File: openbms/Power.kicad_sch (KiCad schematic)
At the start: 17 parts, among them Q6 BSS84AKW,115, Q7 2N7002KW, U20 LMZM23600V3

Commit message: Footprints for pmos/nmos and pmos/pmos packages fixed, charger detection added, pwr_gd and flt_gd lines removed
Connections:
- net PWR_PG: no longer names the net of U20.5 (PG)
- no-connect marks 0 -> 1
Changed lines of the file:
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@@
 		(color 0 0 0 0)
 	)
+	(no_connect
+		(at 170.18 77.47)
+	)
 	(wire
 		(pts
@@
 		(pts
 			(xy 92.71 116.84) (xy 96.52 116.84)
-		)
-		(stroke
-			(width 0)
-			(type default)
-		)
-	)
-	(wire
-		(pts
-			(xy 170.18 77.47) (xy 173.99 77.47)
 		)
 		(stroke
@@
 			)
 			(justify right)
-		)
-	)
-	(hierarchical_label "PWR_PG"
-		(shape output)
-		(at 173.99 77.47 0)
-		(effects
-			(font
-				(size 1.27 1.27)
-				(thickness 0.254)
-				(bold yes)
-				(color 132 0 0 1)
-			)
-			(justify left)
 		)
 	)
@@
 			)
 		)
-		(property "Datasheet" ""
+		(property "Datasheet" "https://www.onsemi.com/pub/Collateral/NDS7002A-D.PDF"
 			(at 121.92 118.11 0)
 			(effects
@@
 			)
 		)
-		(property "Description" ""
+		(property "Description" "0.115A Id, 60V Vds, N-Channel MOSFET, SOT-23"
 			(at 116.84 114.3 0)
 			(effects

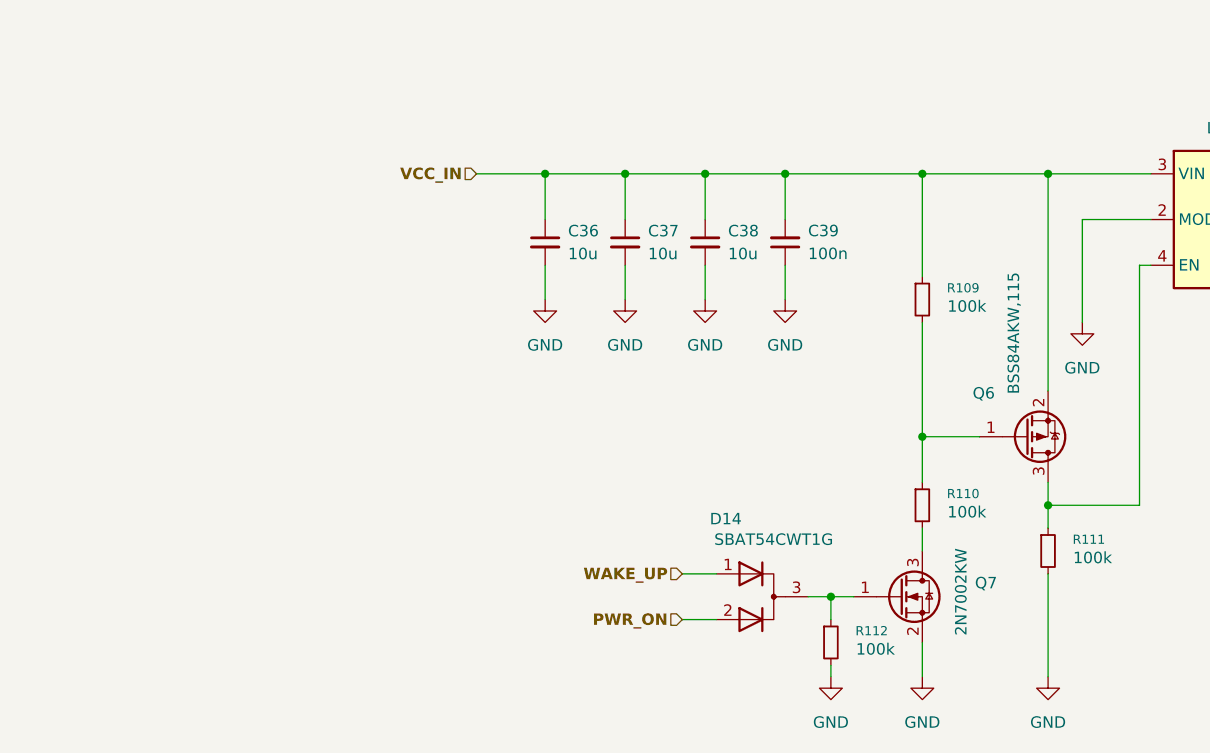
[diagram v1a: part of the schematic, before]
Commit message: Button for quick enable added
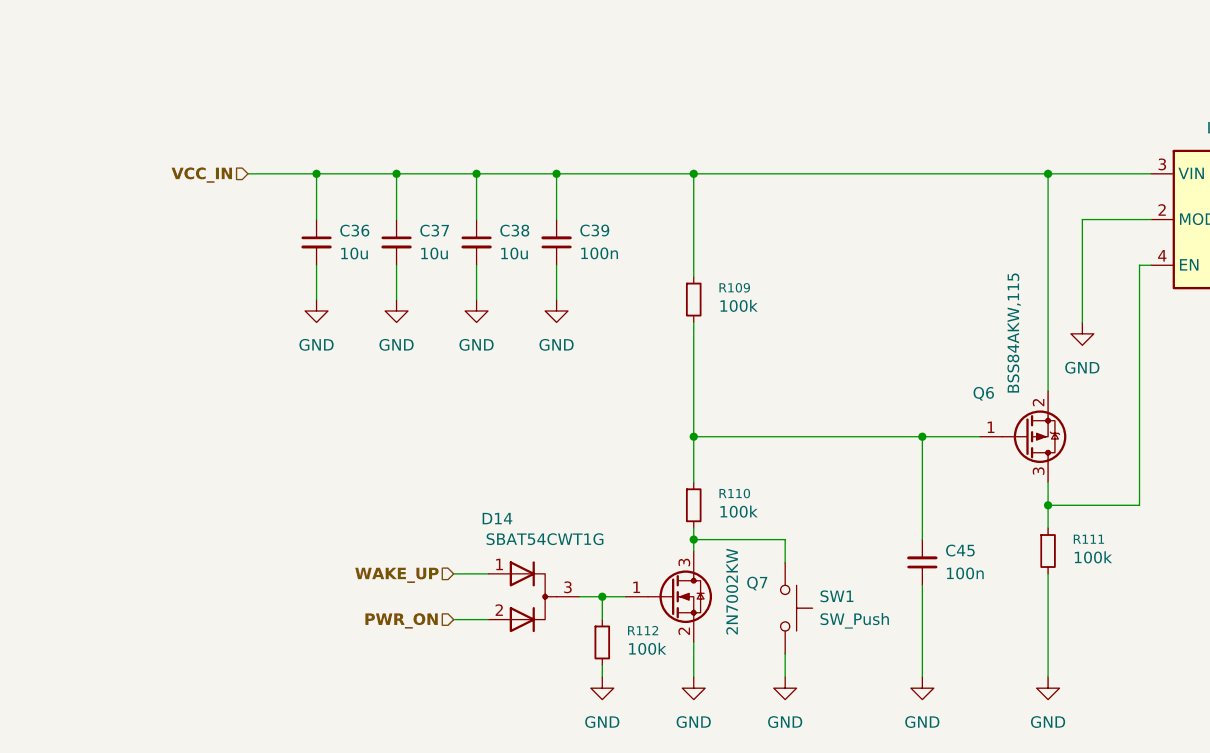
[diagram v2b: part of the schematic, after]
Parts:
- added C45: 100n, Capacitor_SMD:C_0402_1005Metric, symbol Device:C_Small
- added SW1: SW_Push, custom_library:435451019820, symbol Switch:SW_Push
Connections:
- net GND: now also C45.1, SW1.2
- net at Q6.1 (G), R109.2, R110.1: now also C45.2
- net at Q7.3 (D), R110.2: now also SW1.1
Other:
- moved on the sheet: C36, C37, C38, C39, D14, Q7, R109, R110, R112

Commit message: Green LED part number fixed,  PCB mask color updated, project description updated
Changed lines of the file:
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@@
 	(title_block
 		(title "OpenBMS")
-		(date "2026-03-24")
-		(rev "A")
+		(date "2026-09-24")
+		(rev "B")
 		(comment 2 "More at openbatt.dev")
 		(comment 3 "Designed by OpenBatt team")
 		(comment 4 "Open Source Battery Management System")
 	)
-	(text_box "About:\n- Buck converter generates 3.3V out of 4-35V, output up to 500mA. By defult, power converter is off and whole system too. To enable it, signal from outside WAKE_UP needs to be set to 1. After that, once STM32 controller gets on, it can continue keeping power on by setting PWR_ON signal to 1."
+	(text_box "About:\n- Buck converter generates 3.3V out of 4-35V, output up to 500mA. \n- By defult, power converter is off and whole system too. To enable it, signal from outside WAKE_UP needs to be set to 1. After that, once STM32 controller gets on, it can continue keeping power on by setting PWR_ON signal to 1.\n- You can also enable power supply by using on-board switch"
 		(exclude_from_sim no)
 		(at 19.05 17.78 0)
-		(size 81.28 15.24)
+		(size 85.09 15.24)
 		(margins 0.9525 0.9525 0.9525 0.9525)
 		(stroke

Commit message: BOM updates
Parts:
- SW1: value SW_Push -> Button
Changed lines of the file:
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@@
 			)
 		)
-		(property "Value" "SW_Push"
+		(property "Value" "Button"
 			(at 107.95 116.8399 90)
 			(effects
